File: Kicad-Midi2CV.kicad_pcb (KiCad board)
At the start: 2 copper layers, 99.7 x 99.7 mm, 85 parts, among them IC1 MCP4725module, IC2 MCP4725module, J1 Doepfer connector, J10 CV4, J11 Gate1, J12 GateConn, J13 Gate2, J14 Gate3, J15 Gate4, J16 I2C_Conn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

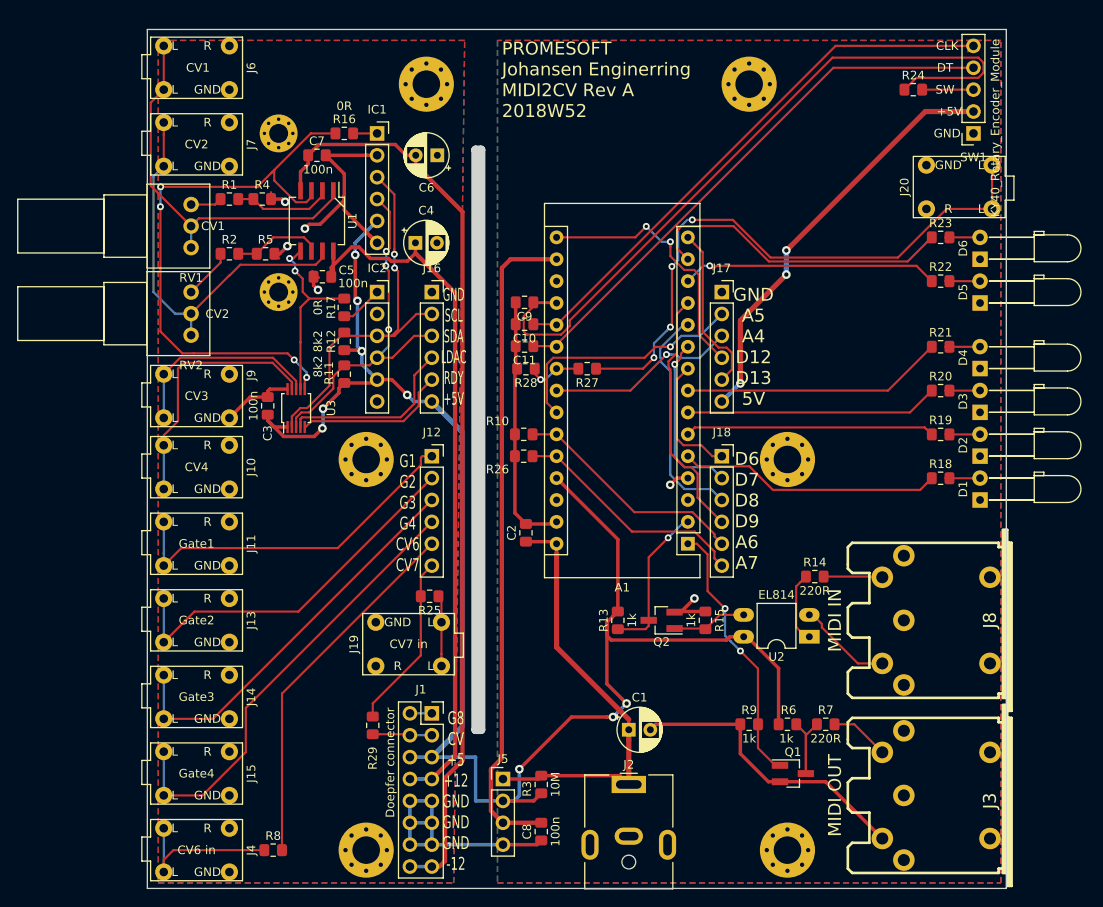
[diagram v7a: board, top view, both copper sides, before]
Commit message: RevA Archived - RevB Initiated
PJ-321 footprint drill increased from 1mm to 1,2mm and rear holes narrower
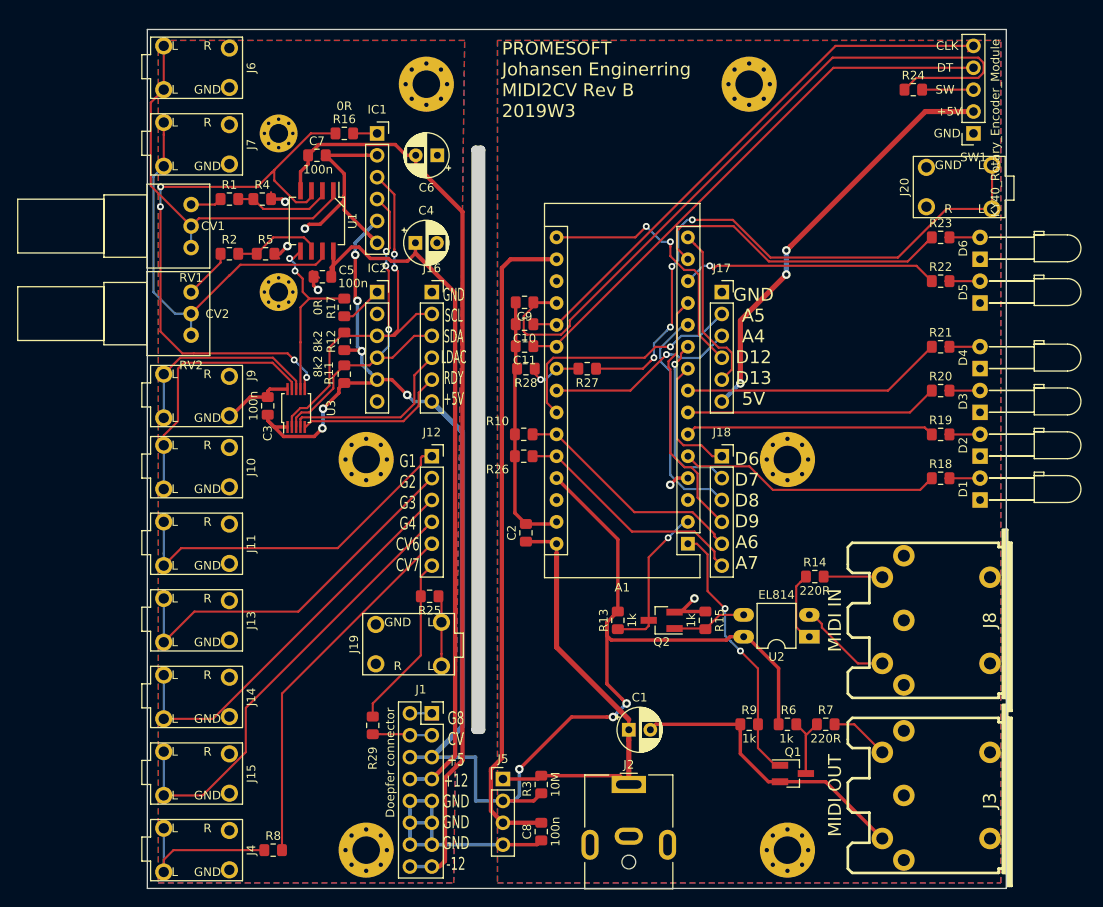
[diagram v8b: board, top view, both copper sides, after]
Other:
- board text added: "PROMESOFT Johansen Enginerring MIDI2CV Rev B 2019W3"
- board text added: "PROMESOFT Johansen Enginerring SubSection - 2019W03 DAC Gate CV RevB"
- board text removed: "PROMESOFT Johansen Enginerring MIDI2CV Rev A 2018W52"
- board text removed: "PROMESOFT Johansen Enginerring SubSection - 2018W52 DAC Gate CV RevA"
